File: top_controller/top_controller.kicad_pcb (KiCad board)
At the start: 2 copper layers, 114 parts, among them J1 OUT1, J10 USB_C_Receptacle_USB2.0, J11 SWD, J12 UART, J13 BOOT0, J14 BOOT1, J2 OUT2, J3 OUT3, J4 OUT4, J5 OUT5, J6 OUT6, J7 OUT7, J8 OUT8, J9 PIN, SW1 RESET, U1 STM32F103C8Tx, U2 LT3045xMSE, U3 AD5754BREZ, U4 AD5754BREZ, U5 REF192, U6 EPM78V2, Y1 8MHz

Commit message: Added second voltage reference
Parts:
- added C28: 0.1uF, Capacitor_SMD:C_0603_1608Metric, F.Cu at (94.8, 61.8)
- added C29: 10uF, Capacitor_SMD:C_1206_3216Metric, F.Cu at (87.2, 68.7)
- added C30: 0.1uF, Capacitor_SMD:C_0603_1608Metric, F.Cu at (94.8, 64.3)
- added TP22: 2v5, TestPoint:TestPoint_Keystone_5010-5014_Multipurpose, F.Cu at (92.5, 69.5)
- added U7: REF192, Package_SO:SOIC-8_3.9x4.9mm_P1.27mm, F.Cu at (87.5, 61.5)
- moved D11 158.1 mm to (252.7, 55.0)
- moved D13 148.7 mm to (210.0, 32.0)
- moved R21 124.6 mm to (249.2, 55.0)
- moved J13 108.4 mm to (191.4, 86.0)
- moved J14 108.3 mm to (195.9, 86.0)
- moved R26 103.2 mm to (211.0, 38.0), turned to -90 degrees
- moved J11 91.9 mm to (200.3, 83.4)
- moved J12 91.9 mm to (205.0, 83.4)
- moved U5 49.6 mm to (184.5, 63.0), turned to 180 degrees
- moved U3 7.68 mm to (162.3, 60.1)
- moved C12 7.52 mm to (171.5, 62.0)
- moved C11 7.50 mm to (248.0, 62.5)
- moved C14 7.50 mm to (229.5, 43.5)
- moved C15 7.50 mm to (235.5, 54.5)
- moved C19 7.50 mm to (249.0, 47.2)
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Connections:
- C18 pad 1: /REF_2V5 -> /REF_2V5_1
- TP14 pad 1: /REF_2V5 -> /REF_2V5_1
- U3 pad 17: /REF_2V5 -> /REF_2V5_1
- U4 pad 17: /REF_2V5 -> /REF_2V5_2
- U5 pad 6: /REF_2V5 -> /REF_2V5_1
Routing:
- net Net-(D13-A): track 0.00 -> 5.20 mm

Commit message: Added capacitors around DC-DC regulator
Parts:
- removed R27, R28: 0R, Resistor_SMD:R_0603_1608Metric
- C24, C27: value 0.1uF -> 10uF; footprint Capacitor_SMD:C_0603_1608Metric -> Capacitor_SMD:C_1206_3216Metric
- C25: value 10uF -> 0.1uF; footprint Capacitor_SMD:C_1206_3216Metric -> Capacitor_SMD:C_0603_1608Metric
- TP4: value AVSS -> GNDA
- TP5: value AVDD -> VDDA
- moved TP13 362.5 mm to (45.0, 49.0)
- moved TP12 353.9 mm to (65.0, 49.0)
- moved TP11 334.6 mm to (85.0, 49.0)
- moved TP10 315.3 mm to (105.0, 49.0)
- moved TP16 308.0 mm to (81.1, 115.1)
- moved TP17 308.0 mm to (81.1, 120.2)
- moved TP18 308.0 mm to (81.1, 125.2)
- moved TP19 308.0 mm to (86.2, 100.0)
- moved TP20 308.0 mm to (86.2, 105.0)
- moved TP21 308.0 mm to (86.2, 110.0)
- moved TP9 296.3 mm to (125.0, 49.0)
- moved TP14 278.6 mm to (141.0, 58.8)
- moved TP8 277.5 mm to (145.0, 49.0)
- moved TP6 259.1 mm to (185.0, 49.0)
- moved TP7 258.9 mm to (165.0, 49.0)
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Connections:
- net Net-(U3-SDO) renamed /SPI_D2D
- C12 pad 2: GND -> GNDA
- C13 pad 2: GND -> GNDA
- C16 pad 1: /AVDD -> VDDA
- C16 pad 2: GND -> GNDA
- C17 pad 1: /AVDD -> VDDA
- C17 pad 2: GND -> GNDA
- C18 pad 2: GND -> GNDA
- C20 pad 1: /AVSS -> VDDA
- C20 pad 2: /AVDD -> GNDA
- C21 pad 2: GND -> GNDA
- C22 pad 1: /AVSS -> VDDA
- C22 pad 2: /AVDD -> GNDA
- C23 pad 2: GND -> GNDA
- C24 pad 1: /PIN_GND -> VDDA
- C24 pad 2: GND -> GNDA
- C25 pad 1: /PIN_GND -> VDDA
- C25 pad 2: GND -> GNDA
- C26 pad 1: /AVSS -> /PIN_VCC
- C26 pad 2: /AVDD -> GNDA
- C27 pad 1: /AVSS -> VDDA
- C27 pad 2: /AVDD -> GNDA
- C28 pad 1: /AVDD -> VDDA
- C28 pad 2: GND -> GNDA
- C29 pad 1: /AVDD -> VDDA
- C29 pad 2: GND -> GNDA
- C30 pad 2: GND -> GNDA
- D11 pad 1: Net-(D11-K) -> GND
- D11 pad 2: +3V3 -> Net-(D11-A)
- D13 pad 1: /PIN_GND -> GNDA
- D14 pad 1: /AVSS -> GNDA
- J1 pad 2: /AVSS -> GNDA
- J2 pad 2: /AVSS -> GNDA
- J3 pad 2: /AVSS -> GNDA
- J4 pad 2: /AVSS -> GNDA
- J5 pad 2: /AVSS -> GNDA
- J6 pad 2: /AVSS -> GNDA
- J7 pad 2: /AVSS -> GNDA
- J8 pad 2: /AVSS -> GNDA
- J9 pad 2: /PIN_GND -> GNDA
- R13 pad 2: GND -> GNDA
- R14 pad 2: GND -> GNDA
- R15 pad 2: GND -> GNDA
- R16 pad 2: GND -> GNDA
- R17 pad 2: GND -> GNDA
- R18 pad 2: GND -> GNDA
- R19 pad 2: GND -> GNDA
- R20 pad 2: GND -> GNDA
- R21 pad 1: GND -> +3V3
- R21 pad 2: Net-(D11-K) -> Net-(D11-A)
- R29 pad 2: /AVDD -> VDDA
- TP4 pad 1: /AVSS -> GNDA
- TP5 pad 1: /AVDD -> VDDA
- U3 pad 1: /AVSS -> GNDA
- U3 pad 15: GND -> GNDA
- U3 pad 18: GND -> GNDA
- U3 pad 19: GND -> GNDA
- U3 pad 20: GND -> GNDA
- U3 pad 21: GND -> GNDA
- U3 pad 24: /AVDD -> VDDA
- U3 pad 25: /AVSS -> GNDA
- U4 pad 1: /AVSS -> GNDA
- U4 pad 15: GND -> GNDA
- U4 pad 18: GND -> GNDA
- U4 pad 19: GND -> GNDA
- U4 pad 20: GND -> GNDA
- U4 pad 21: GND -> GNDA
- U4 pad 24: /AVDD -> VDDA
- U4 pad 25: /AVSS -> GNDA
- U5 pad 2: /AVDD -> VDDA
- U5 pad 3: /AVDD -> VDDA
- U5 pad 4: GND -> GNDA
- U6 pad 2: /AVSS -> GNDA
- U6 pad 3: /AVDD -> VDDA
- U7 pad 2: /AVDD -> VDDA
- U7 pad 3: /AVDD -> VDDA
- U7 pad 4: GND -> GNDA
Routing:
- net /USB_VBUS: track 19.1 -> 0.18 mm
- net GND: track 10.2 -> 0.00 mm, vias 3 -> 0
- net /USB_DP: track 9.67 -> 0.00 mm
- net Net-(D9-K): track 5.38 -> 0.09 mm
- net Net-(D8-K): track 5.38 -> 0.09 mm
- net Net-(D7-K): track 5.38 -> 0.09 mm
- net Net-(D6-K): track 5.38 -> 0.09 mm
- net Net-(D5-K): track 5.38 -> 0.09 mm
- net Net-(D10-K): track 5.38 -> 0.09 mm
- net Net-(D4-K): track 5.20 -> 0.09 mm
- net Net-(D3-K): track 5.20 -> 0.09 mm
- net Net-(D13-A): track 5.20 -> 0.09 mm
- removed copper zone on B.Cu, net GND

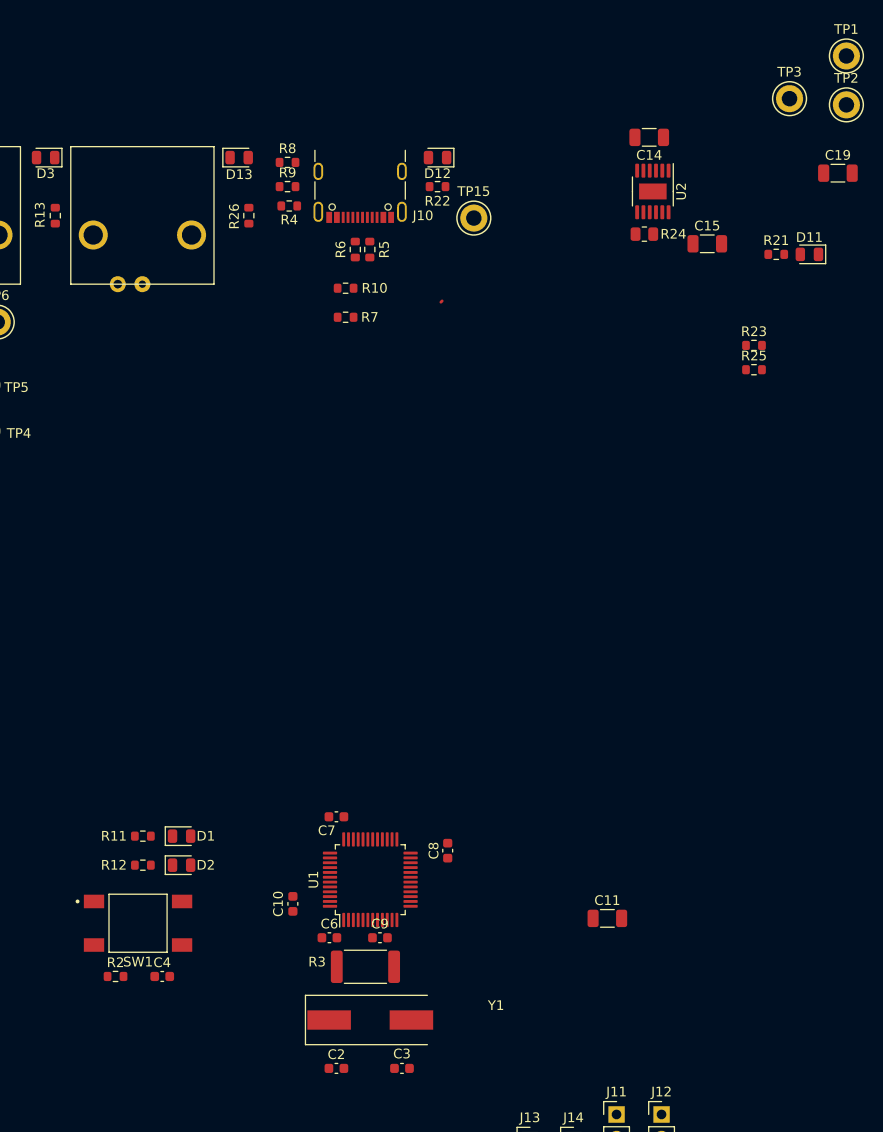
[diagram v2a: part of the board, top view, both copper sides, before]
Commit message: Changed STM LED pins to more convenient ones
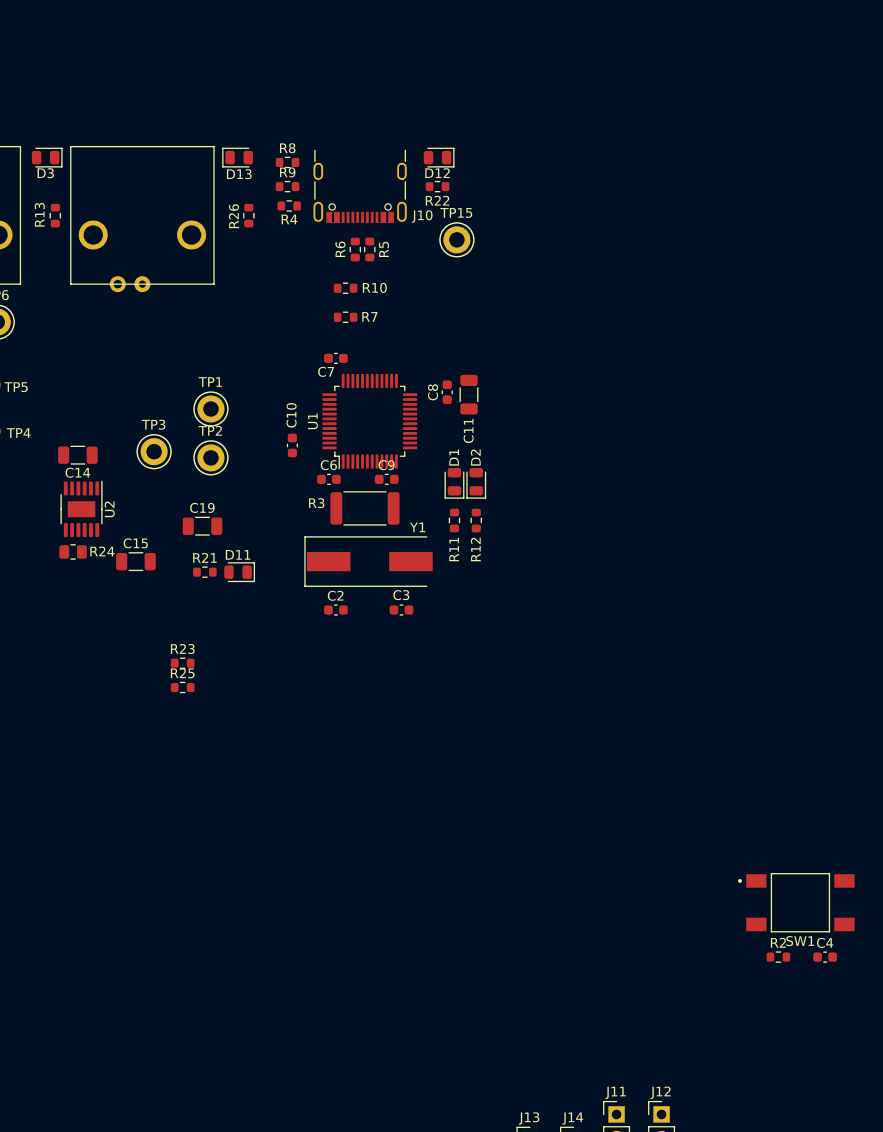
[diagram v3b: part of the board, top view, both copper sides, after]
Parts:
- moved C19 75.1 mm to (206.2, 70.1)
- moved TP1 75.1 mm to (207.1, 58.0)
- moved TP2 75.1 mm to (207.1, 63.0)
- moved TP3 75.1 mm to (201.2, 62.4)
- moved R2 68.5 mm to (265.7, 114.6)
- moved C4 68.5 mm to (270.6, 114.6)
- moved SW1 68.5 mm to (268.0, 109.0)
- moved D11 67.6 mm to (209.9, 74.8)
- moved C14 67.6 mm to (193.3, 62.8)
- moved C15 67.6 mm to (199.3, 73.8)
- moved R21 67.6 mm to (206.5, 74.8)
- moved R23 67.6 mm to (204.2, 84.2)
- moved R24 67.6 mm to (192.8, 72.8)
- moved R25 67.6 mm to (204.2, 86.8)
- moved U2 67.6 mm to (193.7, 68.3)
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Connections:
- U1 pad 18: unconnected-(U1-PB0-Pad18) -> /LED_1
- U1 pad 19: unconnected-(U1-PB1-Pad19) -> /LED_2
- U1 pad 39: /LED_1 -> unconnected-(U1-PB3-Pad39)
- U1 pad 40: /LED_2 -> unconnected-(U1-PB4-Pad40)

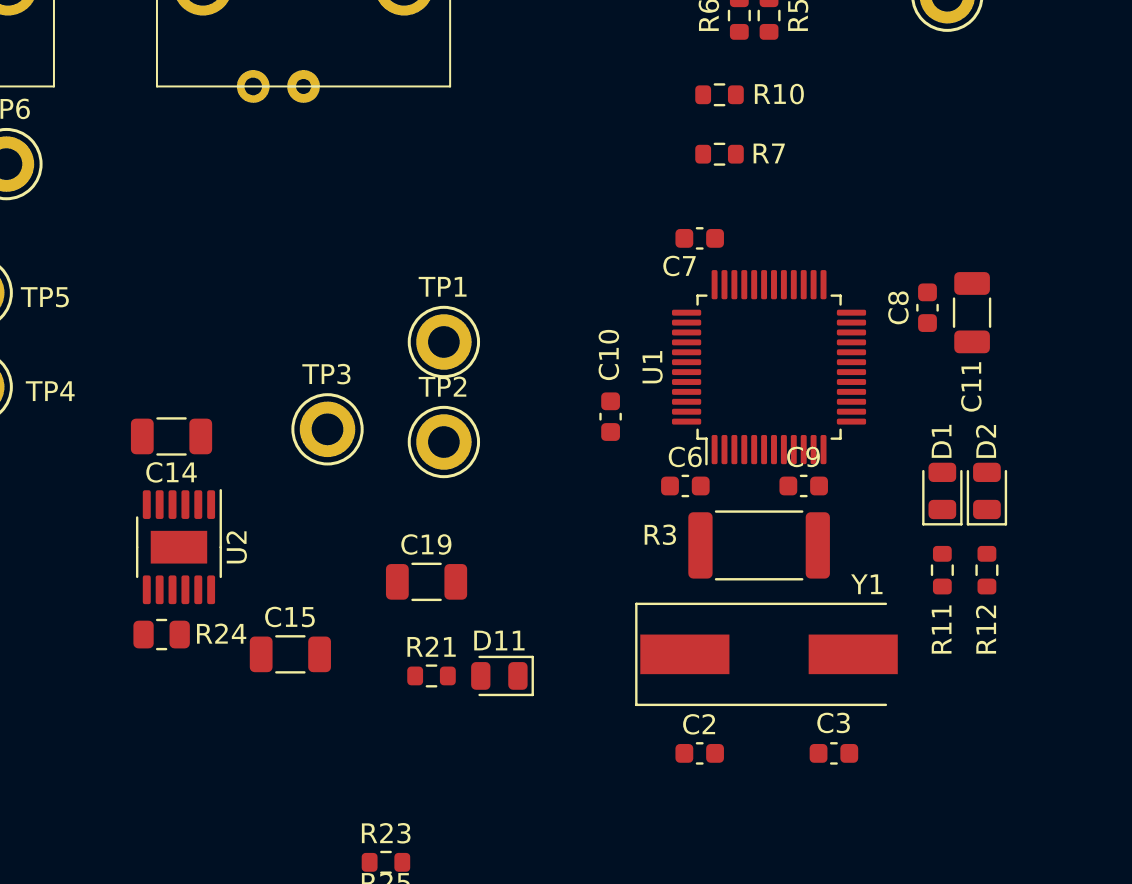
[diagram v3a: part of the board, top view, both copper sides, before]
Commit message: Changed data pins on STM32 for easier tracing
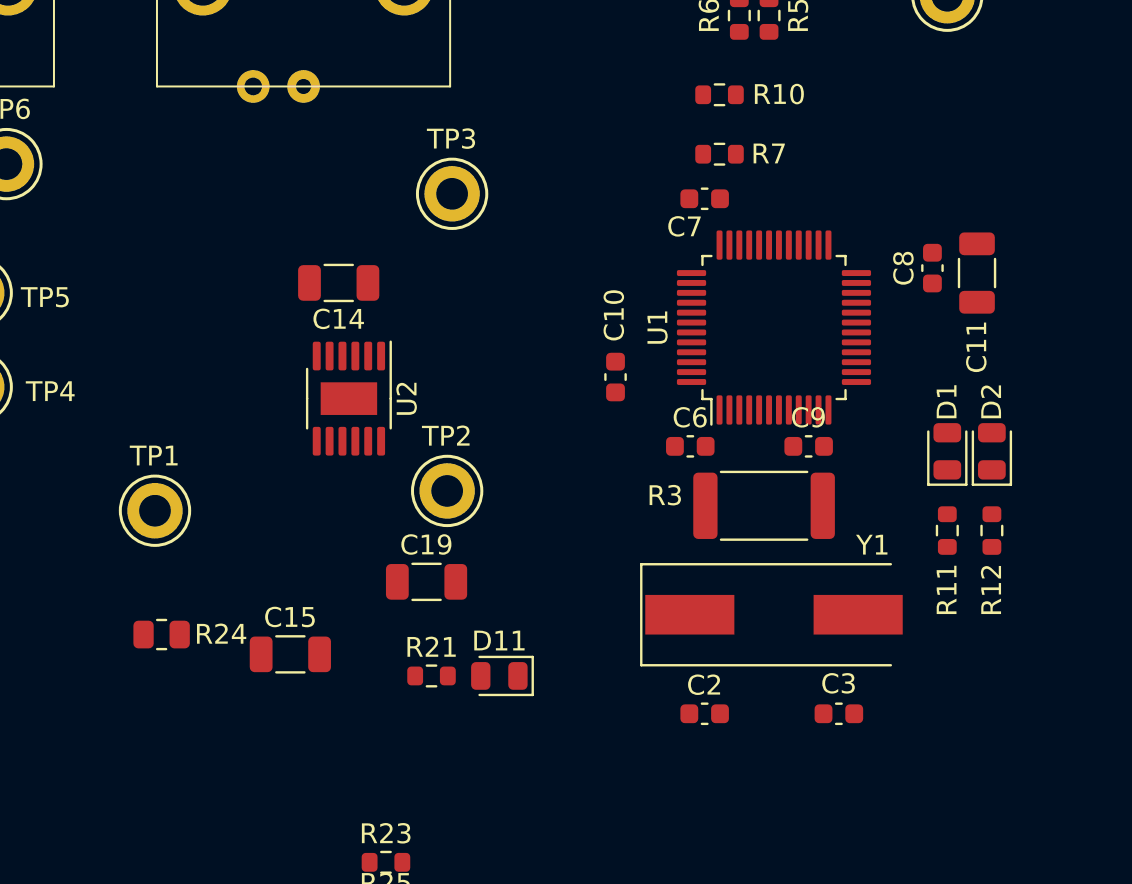
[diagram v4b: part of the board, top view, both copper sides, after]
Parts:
- moved TP1 16.9 mm to (192.5, 66.5)
- moved TP3 13.5 mm to (207.5, 50.5)
- moved C14 11.5 mm to (201.8, 55.0)
- moved U2 11.4 mm to (202.3, 60.8)
- moved TP2 2.48 mm to (207.2, 65.5)
- moved C10 2.02 mm to (215.8, 59.8)
- moved C11 2.02 mm to (234.0, 54.5)
- moved C2 2.02 mm to (220.2, 76.8)
- moved C3 2.02 mm to (227.0, 76.8)
- moved C6 2.02 mm to (219.5, 63.2)
- moved C7 2.02 mm to (220.2, 50.8)
- moved C8 2.02 mm to (231.8, 54.2)
- moved C9 2.02 mm to (225.5, 63.2)
- moved D1 2.02 mm to (232.5, 63.5)
- moved D2 2.02 mm to (234.8, 63.5)
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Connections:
- U1 pad 25: /SPI_NSS -> unconnected-(U1-PB12-Pad25)
- U1 pad 26: /SPI_CLK -> unconnected-(U1-PB13-Pad26)
- U1 pad 27: /SPI_MOSI -> unconnected-(U1-PB14-Pad27)
- U1 pad 28: /SPI_MISO -> unconnected-(U1-PB15-Pad28)
- U1 pad 29: /NLDAC -> unconnected-(U1-PA8-Pad29)
- U1 pad 30: /NCLR -> unconnected-(U1-PA9-Pad30)
- U1 pad 38: unconnected-(U1-PA15-Pad38) -> /SPI_NSS
- U1 pad 39: unconnected-(U1-PB3-Pad39) -> /SPI_SCK
- U1 pad 40: unconnected-(U1-PB4-Pad40) -> /SPI_MISO
- U1 pad 41: unconnected-(U1-PB5-Pad41) -> /SPI_MOSI
- U1 pad 45: unconnected-(U1-PB8-Pad45) -> /NLDAC
- U1 pad 46: unconnected-(U1-PB9-Pad46) -> /NCLR

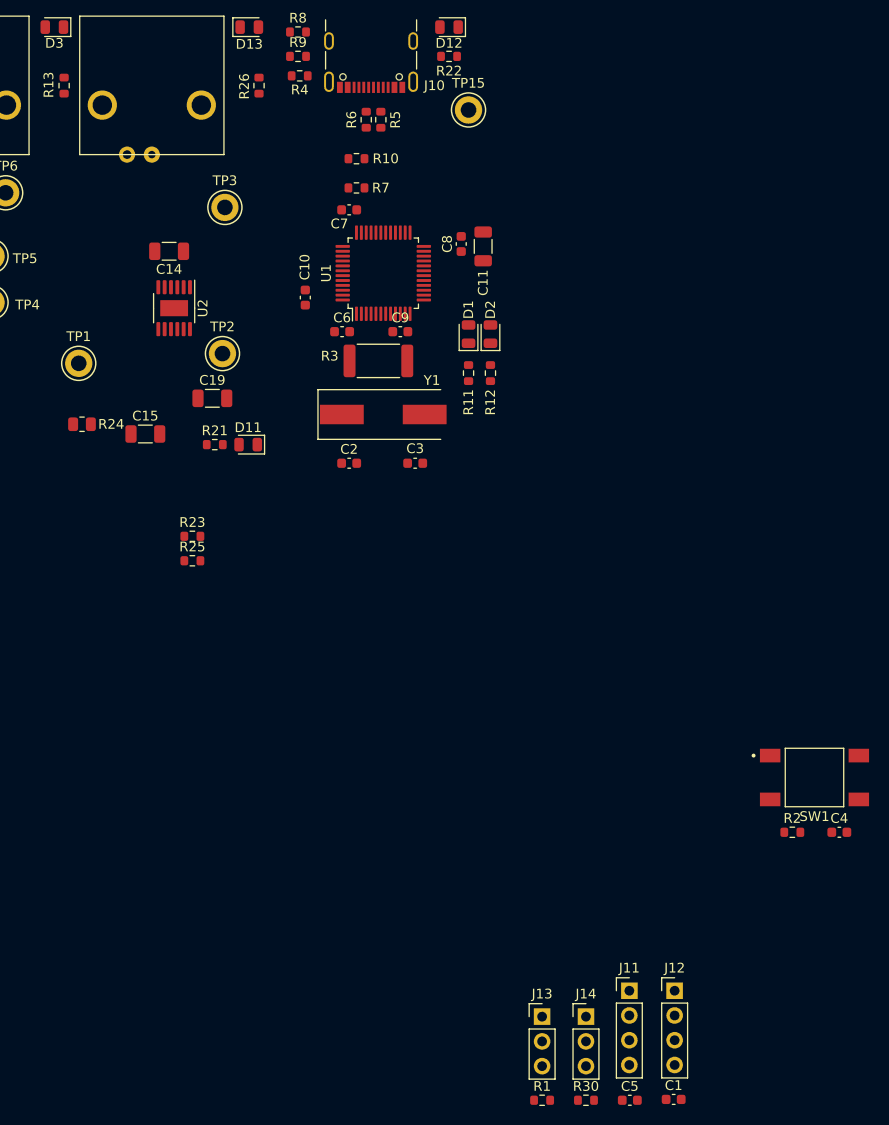
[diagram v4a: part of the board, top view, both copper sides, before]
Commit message: Placed all the components
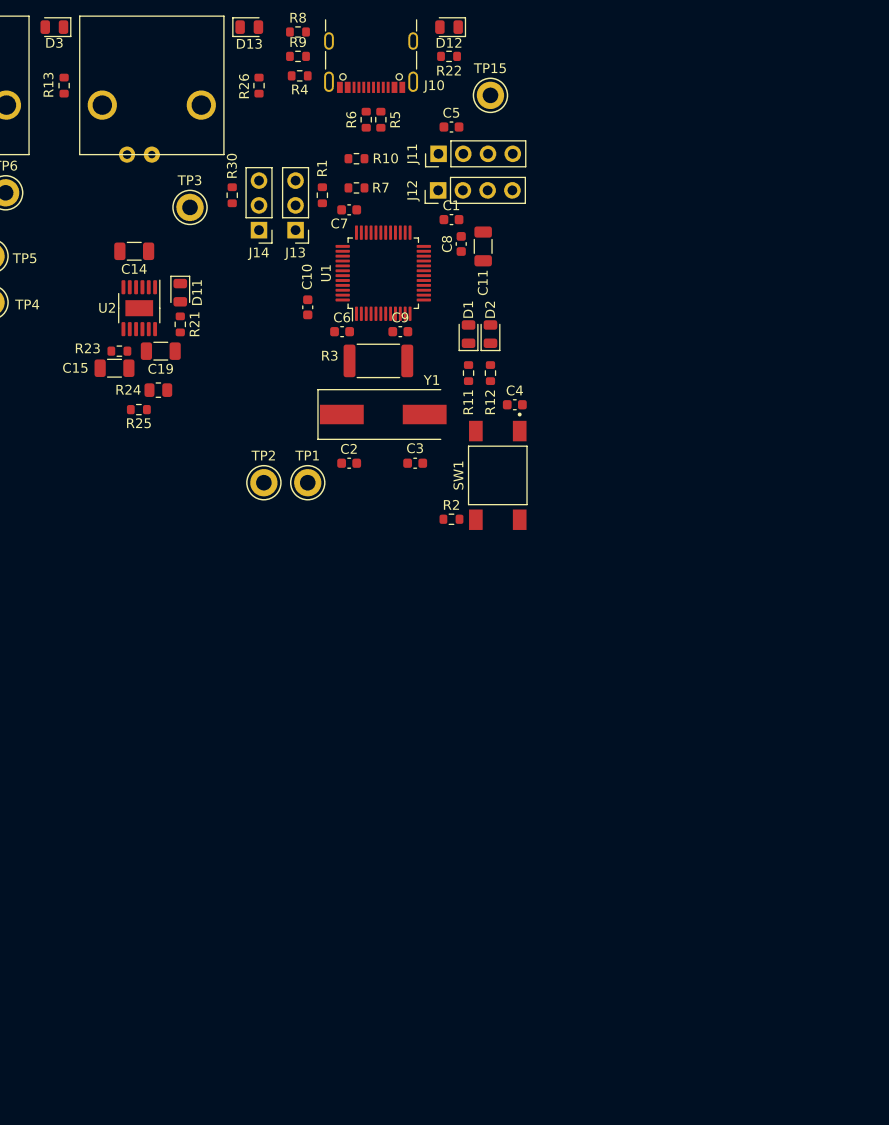
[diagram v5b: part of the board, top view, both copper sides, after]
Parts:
- moved C5 101.5 mm to (230.8, 42.2)
- moved R30 99.7 mm to (208.2, 49.2), turned to -90 degrees
- moved R1 95.6 mm to (217.5, 49.2), turned to -90 degrees
- moved C1 93.1 mm to (230.8, 51.8)
- moved J11 88.1 mm to (229.4, 45.0), turned to 90 degrees
- moved J14 87.4 mm to (211.0, 52.8), turned to 180 degrees
- moved J12 85.6 mm to (229.4, 48.8), turned to 90 degrees
- moved J13 84.6 mm to (214.8, 52.8), turned to 180 degrees
- moved C4 55.1 mm to (237.2, 70.8)
- moved R2 47.5 mm to (230.8, 82.5)
- moved SW1 44.9 mm to (235.5, 78.0), turned to -90 degrees
- moved TP1 26.5 mm to (216.0, 78.8)
- moved R23 20.4 mm to (196.7, 65.2), turned to 180 degrees
- moved D11 17.1 mm to (202.9, 59.2), turned to -90 degrees
- moved R25 16.5 mm to (198.7, 71.2), turned to 180 degrees
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
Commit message: Most of the signals routed
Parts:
- moved TP16 420.3 mm to (499.5, 154.5)
- moved TP17 420.3 mm to (499.5, 159.6)
- moved TP18 420.3 mm to (499.5, 164.6)
- moved TP19 420.3 mm to (504.6, 139.3)
- moved TP20 420.3 mm to (504.6, 144.4)
- moved TP21 420.3 mm to (504.6, 149.4)
- moved C26 19.5 mm to (183.5, 65.2), turned to 90 degrees
- moved TP3 7.19 mm to (196.8, 51.0)
- moved C27 4.95 mm to (167.2, 63.2), turned to 90 degrees
- moved C12 1.83 mm to (128.8, 67.0), turned to 90 degrees
- moved C13 1.62 mm to (126.5, 66.2), turned to 90 degrees
- moved R7 1.03 mm to (221.2, 47.5)
- moved C7 0.25 mm to (220.0, 50.8)
- moved C9 0.25 mm to (225.2, 63.2)
- moved R10 0.25 mm to (221.2, 45.5)
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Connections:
- U1 pad 39: /SPI_SCK -> /SPI_CLK
- U3 pad 22: /OUT_4 -> /OUT_1
- U3 pad 23: /OUT_3 -> /OUT_2
- U3 pad 3: /OUT_1 -> /OUT_3
- U3 pad 4: /OUT_2 -> /OUT_4
- U4 pad 22: /OUT_8 -> /OUT_5
- U4 pad 23: /OUT_7 -> /OUT_6
- U4 pad 3: /OUT_5 -> /OUT_7
- U4 pad 4: /OUT_6 -> /OUT_8
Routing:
- net +3V3: track 0.00 -> 219.9 mm, vias 0 -> 5
- net /LED_CH8: track 0.00 -> 208.1 mm, vias 0 -> 4
- net /LED_CH7: track 0.00 -> 188.1 mm, vias 0 -> 4
- net /LED_CH6: track 0.00 -> 166.2 mm, vias 0 -> 4
- net /LED_CH5: track 0.00 -> 146.2 mm, vias 0 -> 4
- net /SPI_MOSI: track 0.00 -> 128.5 mm, vias 0 -> 2
- net /SPI_CLK: track 0.00 -> 128.3 mm, vias 0 -> 2
- net /SPI_NSS: track 0.00 -> 128.2 mm, vias 0 -> 2
- net /NLDAC: track 0.00 -> 127.4 mm, vias 0 -> 2
- net /LED_CH4: track 0.00 -> 127.2 mm, vias 0 -> 4
- net /NCLR: track 0.00 -> 126.2 mm, vias 0 -> 2
- net /SPI_MISO: track 0.00 -> 114.6 mm, vias 0 -> 2
- net /LED_CH3: track 0.00 -> 105.4 mm, vias 0 -> 4
- net /LED_CH2: track 0.00 -> 84.9 mm, vias 0 -> 4
- net GND: track 0.00 -> 81.9 mm, vias 0 -> 17
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- added copper zone on F.Cu, net GNDA
